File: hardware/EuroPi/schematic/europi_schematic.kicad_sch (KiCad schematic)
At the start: 108 parts, among them J1 Output 1 Jack, J2 Output 2 Jack, J3 Output 3 Jack, J4 Output 4 Jack, J5 Output 5 Jack, J6 Output 6 Jack, J7 Digital Input Jack, J8 Analogue Input Jack, Q1 2N2222, SW1 SW_Push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

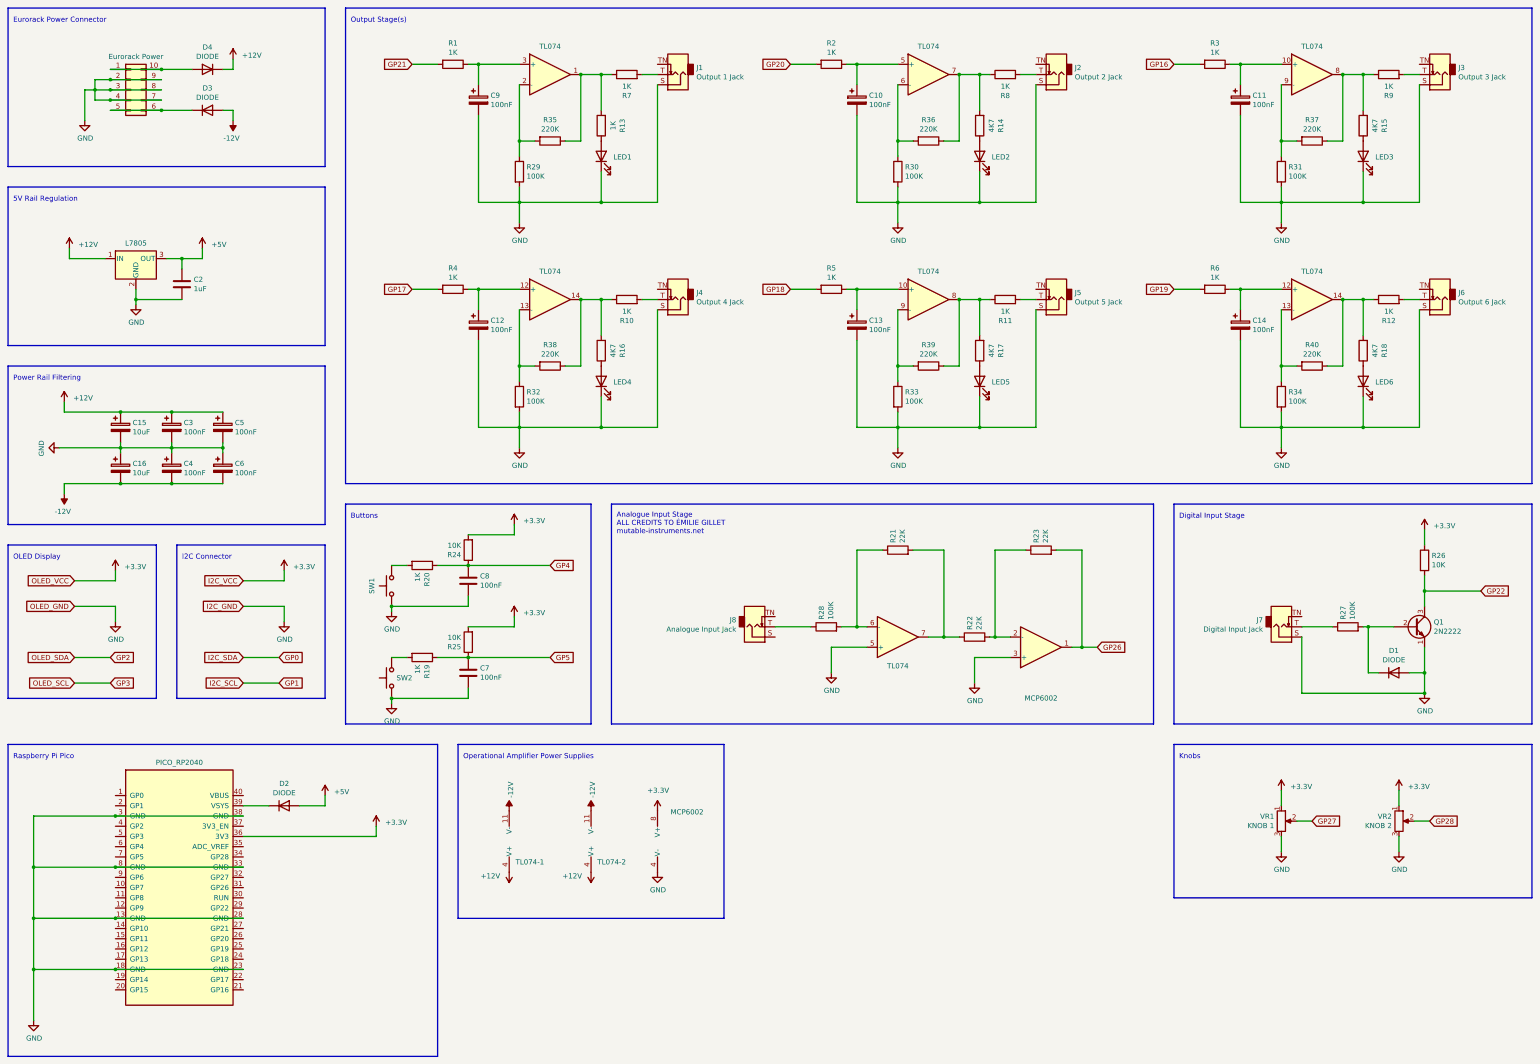
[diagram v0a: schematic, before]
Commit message: Fix errors in schematic (#246)
* Fix errors

R13 value was fixed from 1K to 4K7, and the second MCP6002 unit was specified as unconnected

* Update schematic PDF
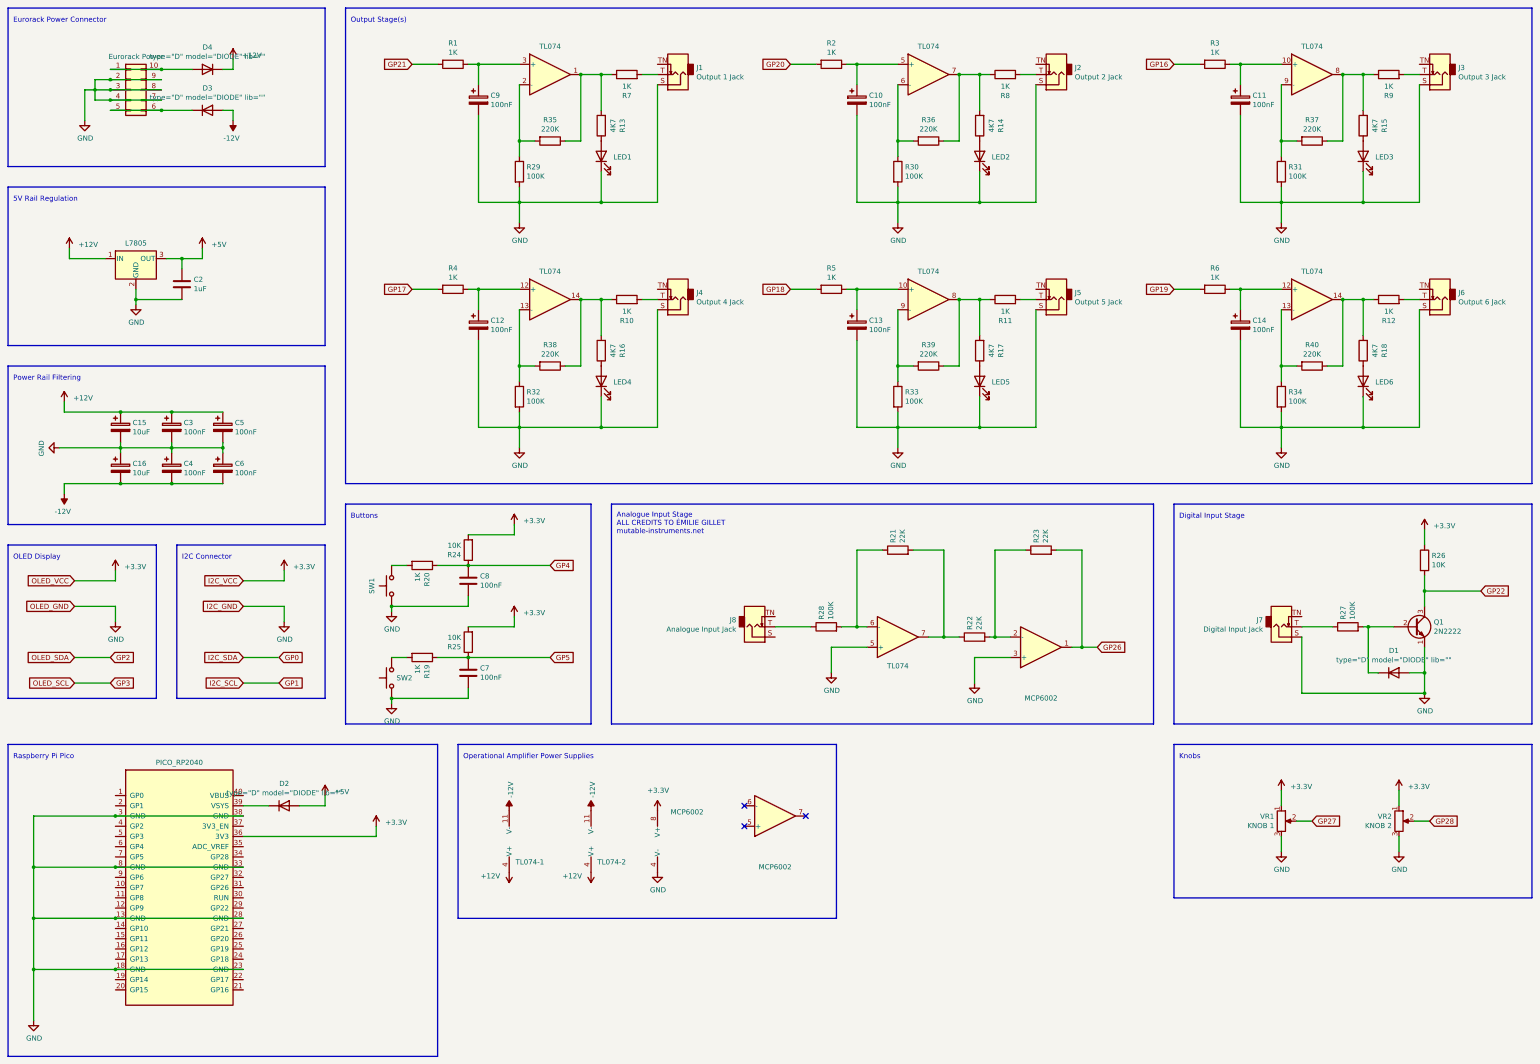
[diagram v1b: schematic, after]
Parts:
- added O1: MCP6002, symbol Amplifier_Operational:MCP6002-xMS
- D1, D2, D3, D4: value DIODE -> ${SIM.PARAMS}; Spice_Netlist_Enabled Y -> (none); Spice_Primitive D -> (none)
- R13: value 1K -> 4K7
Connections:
- no-connect marks 0 -> 3
